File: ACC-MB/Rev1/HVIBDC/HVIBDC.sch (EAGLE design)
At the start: 34 parts, among them IC1 555

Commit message: update
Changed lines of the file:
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@@
 <part name="P-2" library="Main" library_urn="urn:adsk.eagle:library:14107900" deviceset="V-" device=""/>
 <part name="P-4" library="Main" library_urn="urn:adsk.eagle:library:14107900" deviceset="V-" device=""/>
-<part name="U$2" library="ACC-MB-R0" library_urn="urn:adsk.eagle:library:13208985" deviceset="15-24-6100" device=""/>
-<part name="U$1" library="ACC-MB-R0" library_urn="urn:adsk.eagle:library:13208985" deviceset="15-24-6100" device=""/>
+<part name="U$2" library="ACC-MB-R0" library_urn="urn:adsk.eagle:library:13208985" deviceset="15-24-6100" device="" package3d_urn="urn:adsk.eagle:package:14396594/2"/>
+<part name="U$1" library="ACC-MB-R0" library_urn="urn:adsk.eagle:library:13208985" deviceset="15-24-6100" device="" package3d_urn="urn:adsk.eagle:package:14396594/2"/>
 <part name="P-3" library="Main" library_urn="urn:adsk.eagle:library:14107900" deviceset="V-" device=""/>
 <part name="P+4" library="Main" library_urn="urn:adsk.eagle:library:14107900" deviceset="V+" device=""/>
@@
 <text x="209.55" y="95.25" size="3.81" layer="97">Mosfets to drive dashboard troubleshooting
 LEDs, and Accumulator indicator light</text>
-<wire x1="207.01" y1="95.25" x2="295.91" y2="95.25" width="0.1524" layer="97"/>
-<wire x1="207.01" y1="95.25" x2="278.13" y2="63.5" width="0.1524" layer="97"/>
+<wire x1="219.71" y1="101.6" x2="295.91" y2="95.25" width="0.1524" layer="97"/>
 <text x="298.45" y="151.13" size="3.81" layer="97">Clock to generate 4hz TSAL signal</text>
 <text x="299.72" y="232.41" size="3.81" layer="97">Mosfets to drive red TSAL LED</text>

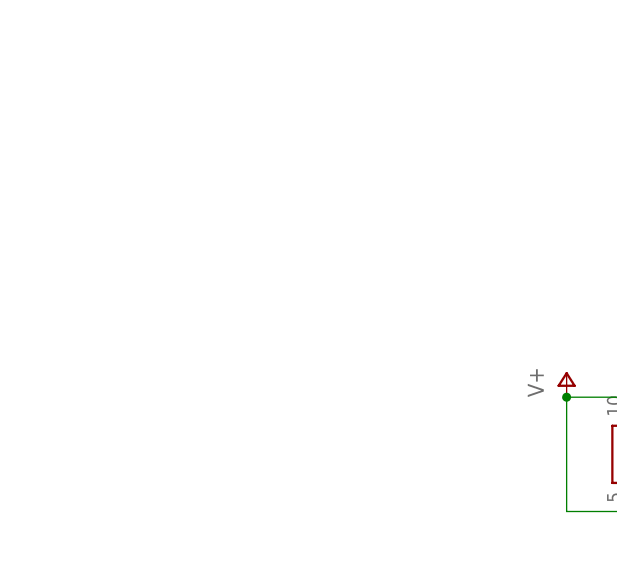
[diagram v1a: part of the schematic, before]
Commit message: 7792 added to all DC
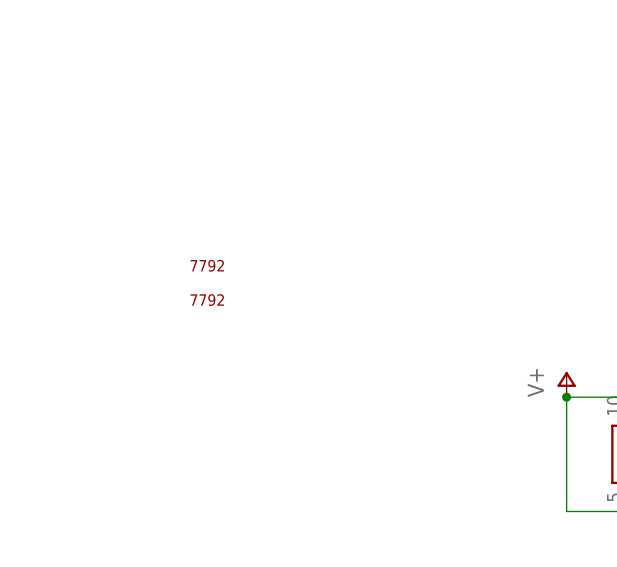
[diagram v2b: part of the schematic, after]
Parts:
- added U$3, U$4: 7792, ACC-MB-R0:7792
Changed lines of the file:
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@@
 <clearance class="0" value="0.1524"/>
 </class>
-<class number="1" name="LVs" width="0" drill="0">
+<class number="1" name="LV" width="0" drill="0">
 <clearance class="1" value="0.0005"/>
 </class>
@@
 <part name="P+1" library="supply1" library_urn="urn:adsk.eagle:library:371" deviceset="+12V" device=""/>
 <part name="GND2" library="supply1" library_urn="urn:adsk.eagle:library:371" deviceset="GND" device=""/>
+<part name="U$3" library="ACC-MB-R0" library_urn="urn:adsk.eagle:library:13208985" deviceset="7792" device="" package3d_urn="urn:adsk.eagle:package:14511284/2"/>
+<part name="U$4" library="ACC-MB-R0" library_urn="urn:adsk.eagle:library:13208985" deviceset="7792" device="" package3d_urn="urn:adsk.eagle:package:14511284/2"/>
 </parts>
 <sheets>
@@
 <attribute name="VALUE" x="355.6" y="49.53" size="1.778" layer="96"/>
 </instance>
+<instance part="U$3" gate="G$1" x="25.4" y="218.44"/>
+<instance part="U$4" gate="G$1" x="25.4" y="214.63"/>
 </instances>
 <busses>
@@
 </segment>
 </net>
-<net name="TSAL_GRN_GND" class="0">
+<net name="TSAL_GRN_GND" class="1">
 <segment>
 <pinref part="R3" gate="G$1" pin="1"/>
@@
 </segment>
 </net>
-<net name="ACC_LGHT" class="0">
+<net name="ACC_LGHT" class="1">
 <segment>
 <wire x1="280.67" y1="58.42" x2="280.67" y2="57.15" width="0.1524" layer="91"/>
@@
 </segment>
 </net>
-<net name="TSAL_RED_GND" class="0">
+<net name="TSAL_RED_GND" class="1">
 <segment>
 <wire x1="300.99" y1="217.17" x2="313.69" y2="217.17" width="0.1524" layer="91"/>
